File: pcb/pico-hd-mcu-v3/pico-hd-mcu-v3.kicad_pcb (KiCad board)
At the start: 2 copper layers, 41 parts

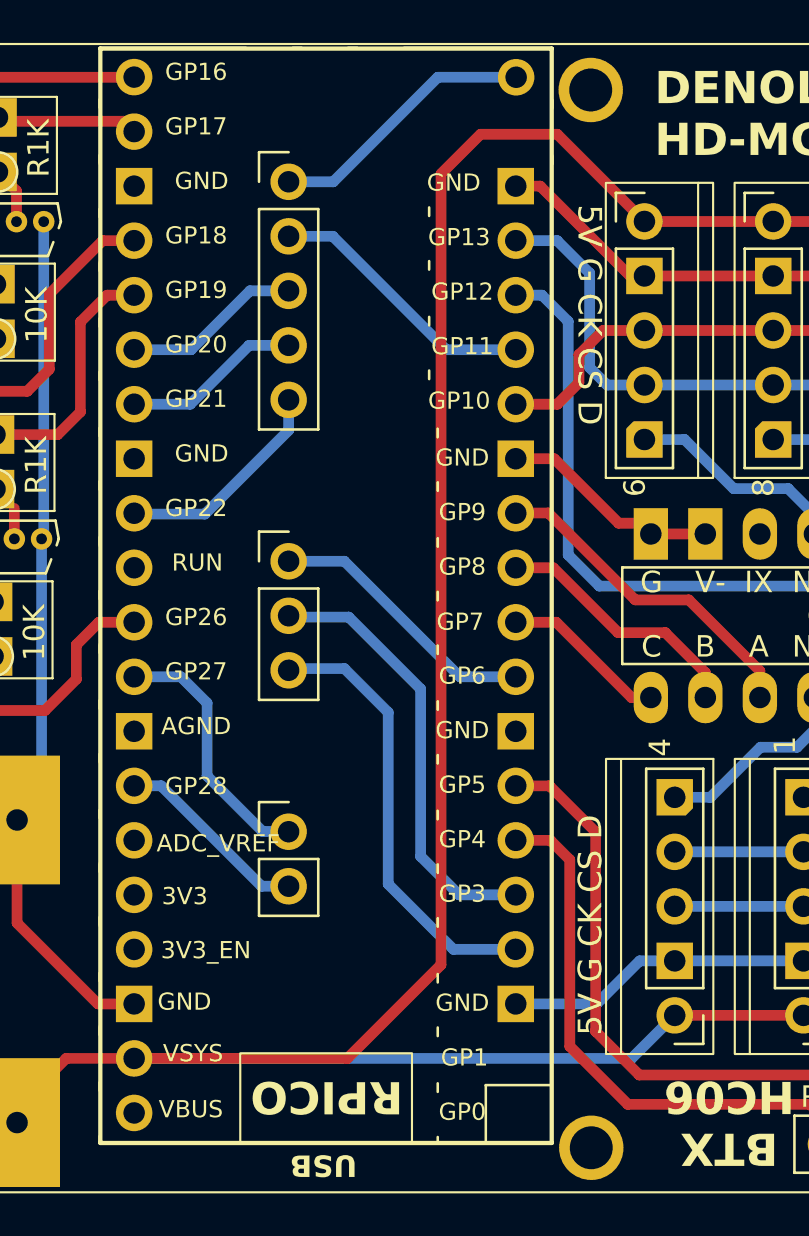
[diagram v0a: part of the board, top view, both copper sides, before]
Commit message: hardware gpio remapping
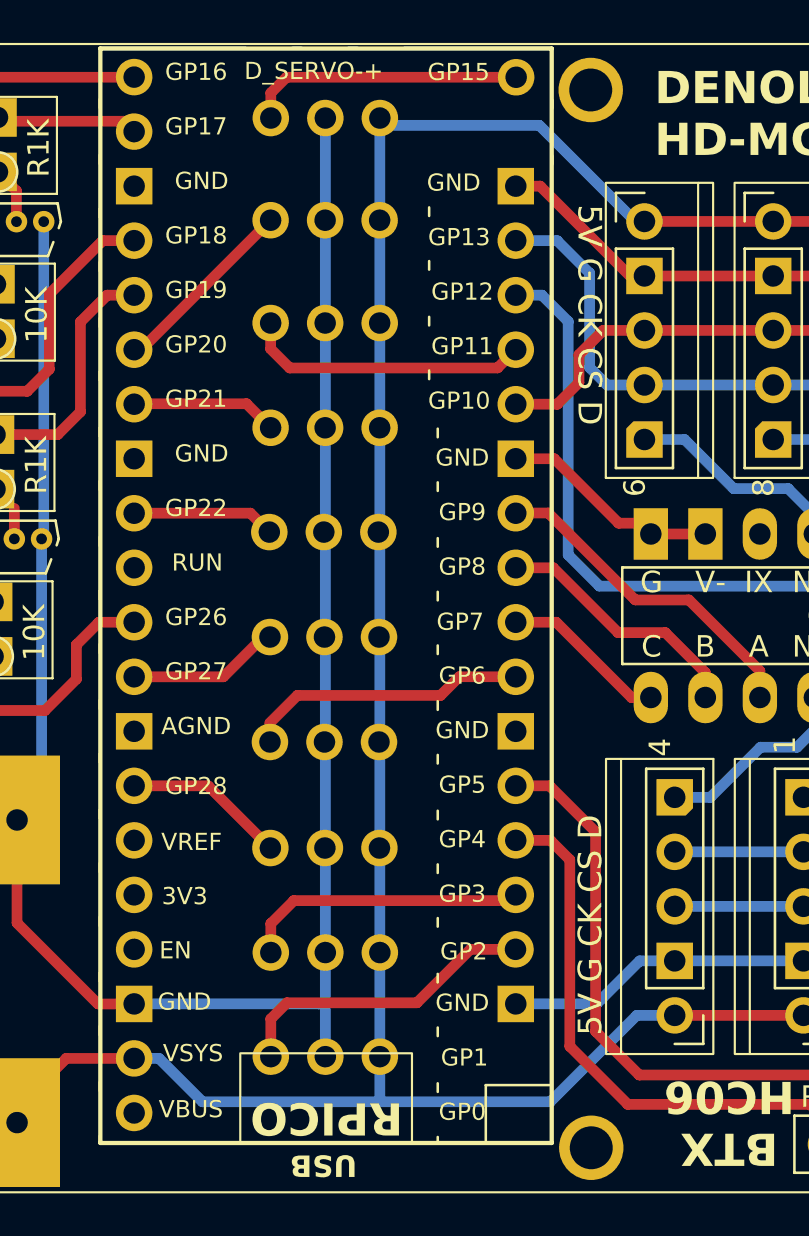
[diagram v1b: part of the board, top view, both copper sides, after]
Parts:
- removed the REF** at (79.6, 27.5)
- removed the REF** at (79.6, 45.2)
- removed the REF** at (79.6, 57.8)
- added REF**: PinHeader_1x03_P2.54mm_Vertical, Connector_PinHeader_2.54mm:PinHeader_1x03_P2.54mm_Vertical, B.Cu at (83.8, 24.6)
- added REF**: PinHeader_1x03_P2.54mm_Vertical, Connector_PinHeader_2.54mm:PinHeader_1x03_P2.54mm_Vertical, B.Cu at (83.8, 53.6)
- added REF**: PinHeader_1x03_P2.54mm_Vertical, Connector_PinHeader_2.54mm:PinHeader_1x03_P2.54mm_Vertical, B.Cu at (83.8, 68.3)
- added REF**: PinHeader_1x03_P2.54mm_Vertical, Connector_PinHeader_2.54mm:PinHeader_1x03_P2.54mm_Vertical, B.Cu at (83.8, 29.3)
- added REF**: PinHeader_1x03_P2.54mm_Vertical, Connector_PinHeader_2.54mm:PinHeader_1x03_P2.54mm_Vertical, B.Cu at (83.8, 34.1)
- added REF**: PinHeader_1x03_P2.54mm_Vertical, Connector_PinHeader_2.54mm:PinHeader_1x03_P2.54mm_Vertical, B.Cu at (83.8, 58.6)
- added REF**: PinHeader_1x03_P2.54mm_Vertical, Connector_PinHeader_2.54mm:PinHeader_1x03_P2.54mm_Vertical, B.Cu at (83.8, 39.0)
- added REF**: PinHeader_1x03_P2.54mm_Vertical, Connector_PinHeader_2.54mm:PinHeader_1x03_P2.54mm_Vertical, B.Cu at (83.8, 43.8)
- added REF**: PinHeader_1x03_P2.54mm_Vertical, Connector_PinHeader_2.54mm:PinHeader_1x03_P2.54mm_Vertical, B.Cu at (83.8, 48.7)
- added REF**: PinHeader_1x03_P2.54mm_Vertical, Connector_PinHeader_2.54mm:PinHeader_1x03_P2.54mm_Vertical, B.Cu at (83.8, 63.4)
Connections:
- ? pad 20: AUX_G15 -> D_SERVO_PWM
- ? pad 4: AUX_G2 -> D_IGN
- REF** pad 15: AUX_G11 -> D_SPEED
- REF** pad 34: AUX_A2 -> D_HALL
- REF** pad 5: AUX_G3 -> D_RPM
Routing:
- net GND: track 190.7 -> 243.4 mm
- net AUX_G2: track 20.7 -> 0.00 mm
- net AUX_G3: track 20.5 -> 0.00 mm
- net D_IGN: track 0.00 -> 14.5 mm
- net D_SPEED: track 0.00 -> 13.3 mm
- net D_RPM: track 0.00 -> 13.3 mm
- net D_SERVO_PWM: track 0.00 -> 12.9 mm
- net AUX_G11: track 12.8 -> 0.00 mm
- net AUX_G15: track 12.6 -> 0.00 mm
- net AUX_A2: track 9.14 -> 0.00 mm
- net D_HALL: track 0.00 -> 7.55 mm
- net AUX_A1: track 12.2 -> 6.91 mm
- net AUX_G22: track 10.2 -> 6.66 mm
- net 5V: track 155.7 -> 152.6 mm
- net AUX_G21: track 8.33 -> 6.80 mm
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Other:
- board text added: "D_HALL"
- board text added: "D_IGN"
- board text added: "D_RPM"
- board text added: "D_SERVO-+"
- board text added: "D_SPEED"
- board text added: "G20"
- board text added: "G21"
- board text added: "G22"
- board text added: "G27A1"
- board text added: "G6"
- board text added: "GP15"
- board text added: "GP2"
- board text removed: "AUX_G11"
- board text removed: "AUX_G15"
- board text removed: "AUX_G2"
- board text removed: "AUX_G20"
- board text removed: "AUX_G21"
- board text removed: "AUX_G22"
- board text removed: "AUX_G27 A1"
- board text removed: "AUX_G28 A2"
- board text removed: "AUX_G3"
- board text removed: "AUX_G6"

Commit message: update pcb v3
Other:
- board outline added: 82.4 x 53.6 mm
- board text added: "D_SERVO"
- board text removed: "D_SERVO-+"
- board text removed: "EXT"

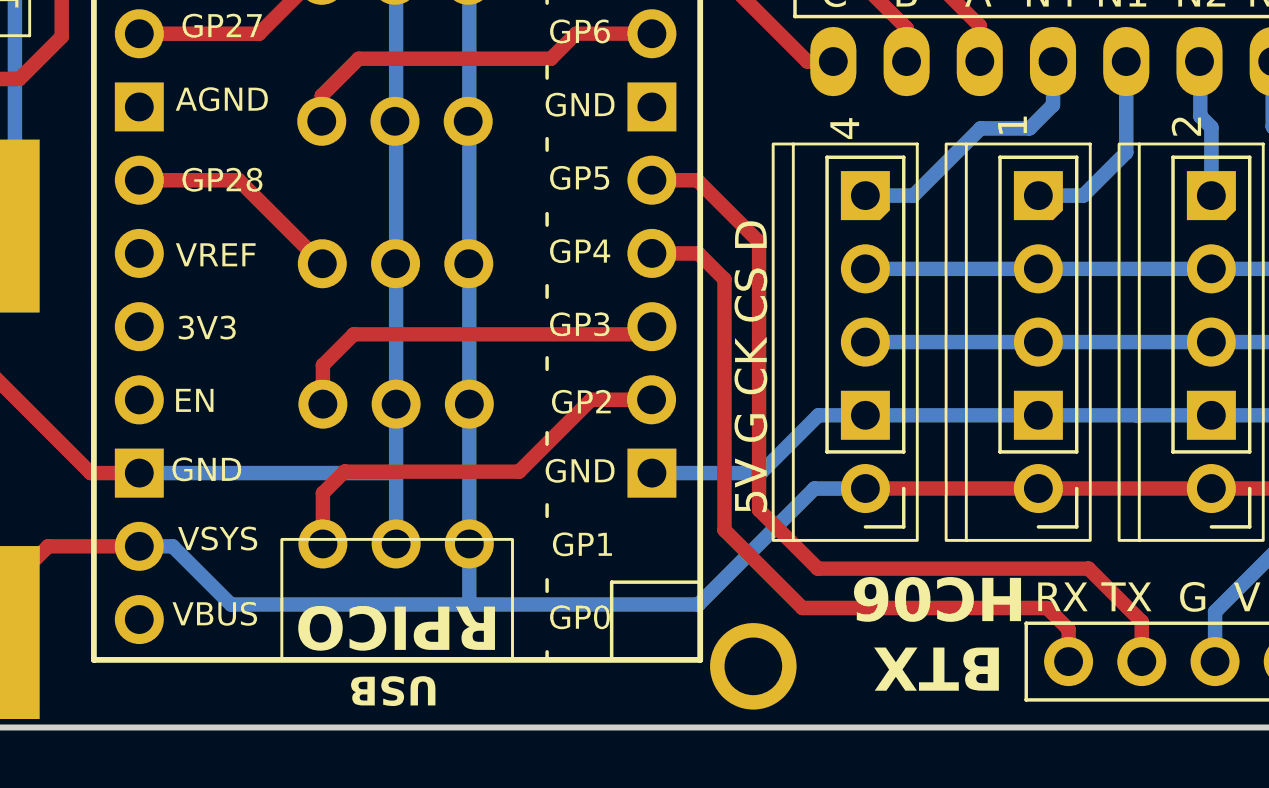
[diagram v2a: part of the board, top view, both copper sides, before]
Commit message: fallback to uart0 for bt rx/tx
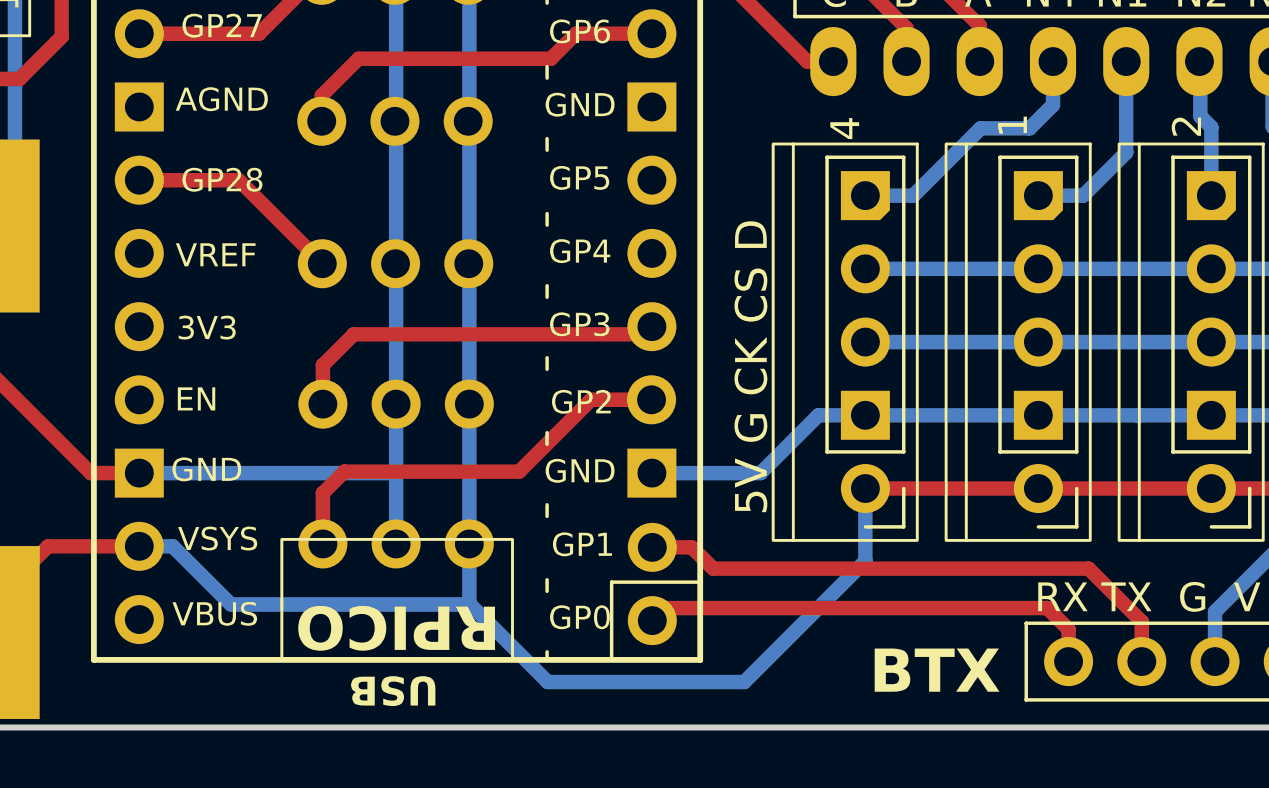
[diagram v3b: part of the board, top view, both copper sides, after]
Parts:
- removed the ? at (93.7, 72.5)
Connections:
- REF** pad 6: D_BT_TX -> AUX_G4
- REF** pad 7: D_BT_RX -> AUX_G5
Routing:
- net D_BT_RX: track 30.2 -> 19.4 mm
- net D_BT_TX: track 26.1 -> 16.0 mm
- net 5V: track 152.6 -> 156.3 mm
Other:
- board text added: "BTX"
- board text removed: "BTX HC06"
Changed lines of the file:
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@@
 	(net 37 "D_SPEED")
 	(net 38 "D_HALL")
+	(net 39 "AUX_G4")
+	(net 40 "AUX_G5")
 	(footprint "Resistor_THT:R_Axial_DIN0204_L3.6mm_D1.6mm_P2.54mm_Vertical"
 		(layer "F.Cu")
@@
 		)
 		(fp_text user "EN"
-			(at 7.7765 -17.2075 0)
+			(at 7.7165 -17.1575 0)
 			(layer "F.SilkS")
 			(effects
@@
 			(layers)
 		)
+		(pad "1" thru_hole oval
+			(at -8.85 -24.8165 180)
+			(size 1.7 1.7)
+			(drill 1)
+			(layers "*.Cu" "*.Mask")
+			(remove_unused_layers no)
+			(net 24 "D_BT_TX")
+		)
+		(pad "2" thru_hole oval
+			(at -8.85 -22.2765 180)
+			(size 1.7 1.7)
+			(drill 1)
+			(layers "*.Cu" "*.Mask")
+			(remove_unused_layers no)
+			(net 23 "D_BT_RX")
+		)
 		(pad "3" thru_hole rect
 			(at -8.836 -19.7 180)
@@
 			(layers "*.Cu" "*.Mask")
 			(remove_unused_layers no)
-			(net 24 "D_BT_TX")
+			(net 39 "AUX_G4")
 		)
 		(pad "7" thru_hole oval
@@
 			(layers "*.Cu" "*.Mask")
 			(remove_unused_layers no)
-			(net 23 "D_BT_RX")
+			(net 40 "AUX_G5")
 		)
 		(pad "8" thru_hole rect
@@
 		(embedded_fonts no)
 	)
-	(footprint ""
-		(layer "F.Cu")
-		(at 93.7 72.525)
-		(property "Reference" ""
-			(at 0 0 0)
-			(layer "F.SilkS")
-			(effects
-				(font
-					(size 1.27 1.27)
-					(thickness 0.15)
-				)
-			)
-		)
-		(property "Value" ""
-			(at 0 0 0)
-			(layer "F.SilkS")
-			(effects
-				(font
-					(size 1.27 1.27)
-					(thickness 0.15)
-				)
-			)
-		)
-		(property "Datasheet" ""
-			(at 0 0 0)
-			(layer "F.Fab")
-			(hide yes)
-			(effects
-				(font
-					(size 1.27 1.27)
-					(thickness 0.15)
-				)
-			)
-		)
-		(property "Description" ""
-			(at 0 0 0)
-			(layer "F.Fab")
-			(hide yes)
-			(effects
-				(font
-					(size 1.27 1.27)
-					(thickness 0.15)
-				)
-			)
-		)
-		(pad "1" thru_hole circle
-			(at 0 0)
-			(size 3 3)
-			(drill 2)
-			(layers "*.Cu" "*.Mask")
-			(remove_unused_layers no)
-		)
-		(embedded_fonts no)
-	)
 	(footprint "Package_TO_SOT_SMD:SOT-223"
 		(layer "F.Cu")
@@
 		)
 	)
-	(gr_text "BTX\nHC06"
-		(at 100.1275 69.2725 180)
+	(gr_text "BTX"
+		(at 100 73.59 0)
 		(layer "F.SilkS" knockout)
 		(effects
@@
 		)
 	)
-	(gr_text "BTX\nHC06"
+	(gr_text "BTX"
 		(at 100.1275 73.5825 0)
 		(layer "B.SilkS" knockout)
@@
 	)
 	(segment
+		(start 86.57 73.07)
+		(end 93.39 73.07)
+		(width 0.5)
+		(layer "B.Cu")
+		(net 7)
+	)
+	(segment
 		(start 95.7575 29.3675)
 		(end 91.28 24.89)
@@
 	)
 	(segment
-		(start 91.796447 70.38)
-		(end 95.818947 66.3575)
+		(start 72.4025 68.3625)
+		(end 73.5625 68.3625)
 		(width 0.5)
 		(layer "B.Cu")
@@
 	)
 	(segment
-		(start 72.4025 68.3625)
-		(end 73.5625 68.3625)
+		(start 97.5875 68.8725)
+		(end 97.5875 66.3575)
 		(width 0.5)
 		(layer "B.Cu")
@@
 	)
 	(segment
-		(start 95.818947 66.3575)
-		(end 97.5875 66.3575)
+		(start 93.39 73.07)
+		(end 97.5875 68.8725)
+		(width 0.5)
+		(layer "B.Cu")
+		(net 7)
+	)
+	(segment
+		(start 83.86 70.38)
+		(end 83.88 70.38)
 		(width 0.5)
 		(layer "B.Cu")
@@
 	)
 	(segment
-		(start 83.86 70.38)
-		(end 91.796447 70.38)
+		(start 83.88 70.38)
+		(end 86.57 73.07)
 		(width 0.5)
 		(layer "B.Cu")
@@
 	)
 	(segment
-		(start 91.7575 55.6625)
-		(end 90.1825 55.6625)
-		(width 0.5)
-		(layer "F.Cu")
-		(net 23)
-	)
-	(segment
-		(start 107.175 72.36)
-		(end 107.175 70.98)
-		(width 0.5)
-		(layer "F.Cu")
-		(net 23)
-	)
-	(segment
-		(start 93.9 67.1)
-		(end 93.9 57.805)
+		(start 105.33 69.135)
+		(end 92.305 69.135)
 		(width 0.5)
 		(layer "F.Cu")
@@
 	)
 	(segment
-		(start 93.9 57.805)
-		(end 91.7575 55.6625)
+		(start 107.175 70.98)
+		(end 105.33 69.135)
 		(width 0.5)
 		(layer "F.Cu")
@@
 	)
 	(segment
-		(start 95.935 69.135)
-		(end 93.9 67.1)
+		(start 91.569 68.399)
+		(end 90.1965 68.399)
 		(width 0.5)
 		(layer "F.Cu")
@@
 	)
 	(segment
-		(start 105.33 69.135)
-		(end 95.935 69.135)
+		(start 92.305 69.135)
+		(end 91.569 68.399)
 		(width 0.5)
 		(layer "F.Cu")
@@
 	)
 	(segment
-		(start 107.175 70.98)
-		(end 105.33 69.135)
+		(start 107.175 72.36)
+		(end 107.175 70.98)
 		(width 0.5)
 		(layer "F.Cu")
@@
 	)
 	(segment
-		(start 104.635 71.24)
-		(end 103.8975 70.5025)
+		(start 104.635 72.36)
+		(end 104.635 71.24)
 		(width 0.5)
 		(layer "F.Cu")
@@
 	(segment
 		(start 103.8975 70.5025)
-		(end 95.4025 70.5025)
-		(width 0.5)
-		(layer "F.Cu")
-		(net 24)
-	)
-	(segment
-		(start 92.7 59.105)
-		(end 91.7975 58.2025)
-		(width 0.5)
-		(layer "F.Cu")
-		(net 24)
-	)
-	(segment
-		(start 95.4025 70.5025)
-		(end 92.7 67.8)
-		(width 0.5)
-		(layer "F.Cu")
-		(net 24)
-	)
-	(segment
-		(start 92.7 67.8)
-		(end 92.7 59.105)
+		(end 90.633 70.5025)
 		(width 0.5)
 		(layer "F.Cu")
@@
 	)
 	(segment
-		(start 91.7975 58.2025)
-		(end 90.1825 58.2025)
+		(start 104.635 71.24)
+		(end 103.8975 70.5025)
 		(width 0.5)
 		(layer "F.Cu")
@@
 	)
 	(segment
-		(start 104.635 72.36)
-		(end 104.635 71.24)
+		(start 90.633 70.5025)
+		(end 90.1965 70.939)
 		(width 0.5)
 		(layer "F.Cu")
